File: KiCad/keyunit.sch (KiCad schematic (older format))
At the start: 22 parts, among them J1 Conn_01x03_Male, J2 Conn_01x02_Male, J3 Conn_01x05_Male, J4 Conn_01x04_Male, J5 Conn_01x05_Male, J6 Conn_01x04_Male, J8 Conn_01x02_Male, SW0 SW_Push, SW1 SW_Push, U1 test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

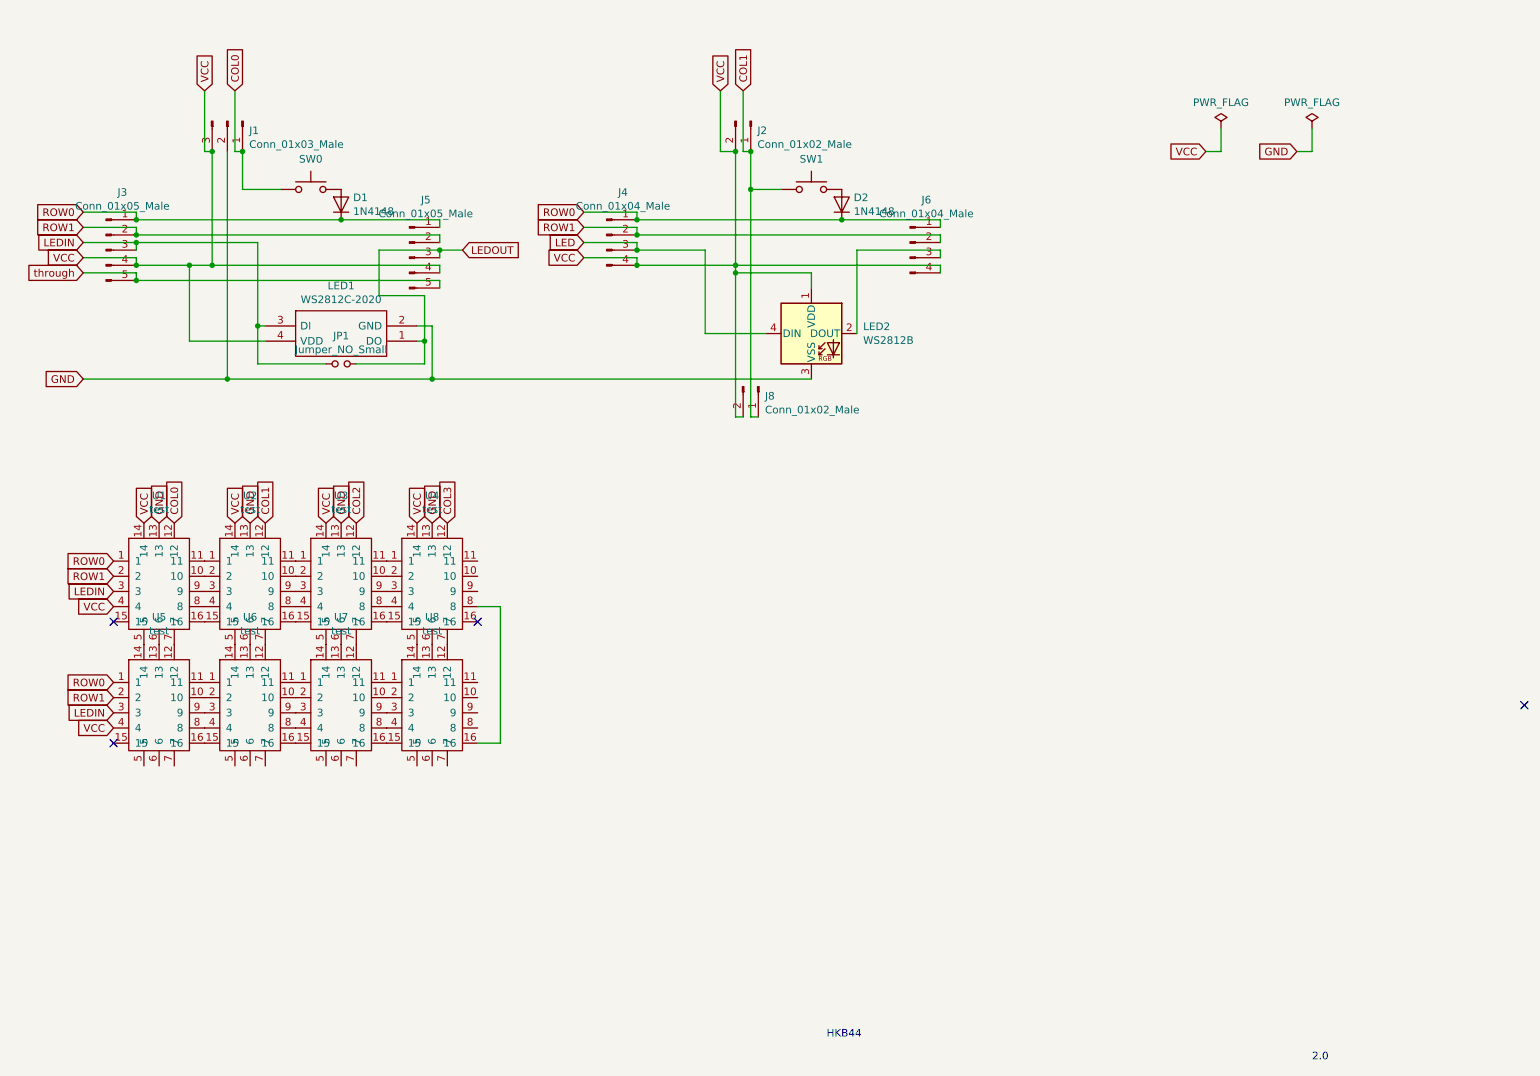
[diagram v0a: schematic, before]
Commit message: Add keyunit foot print and keyunit2 board
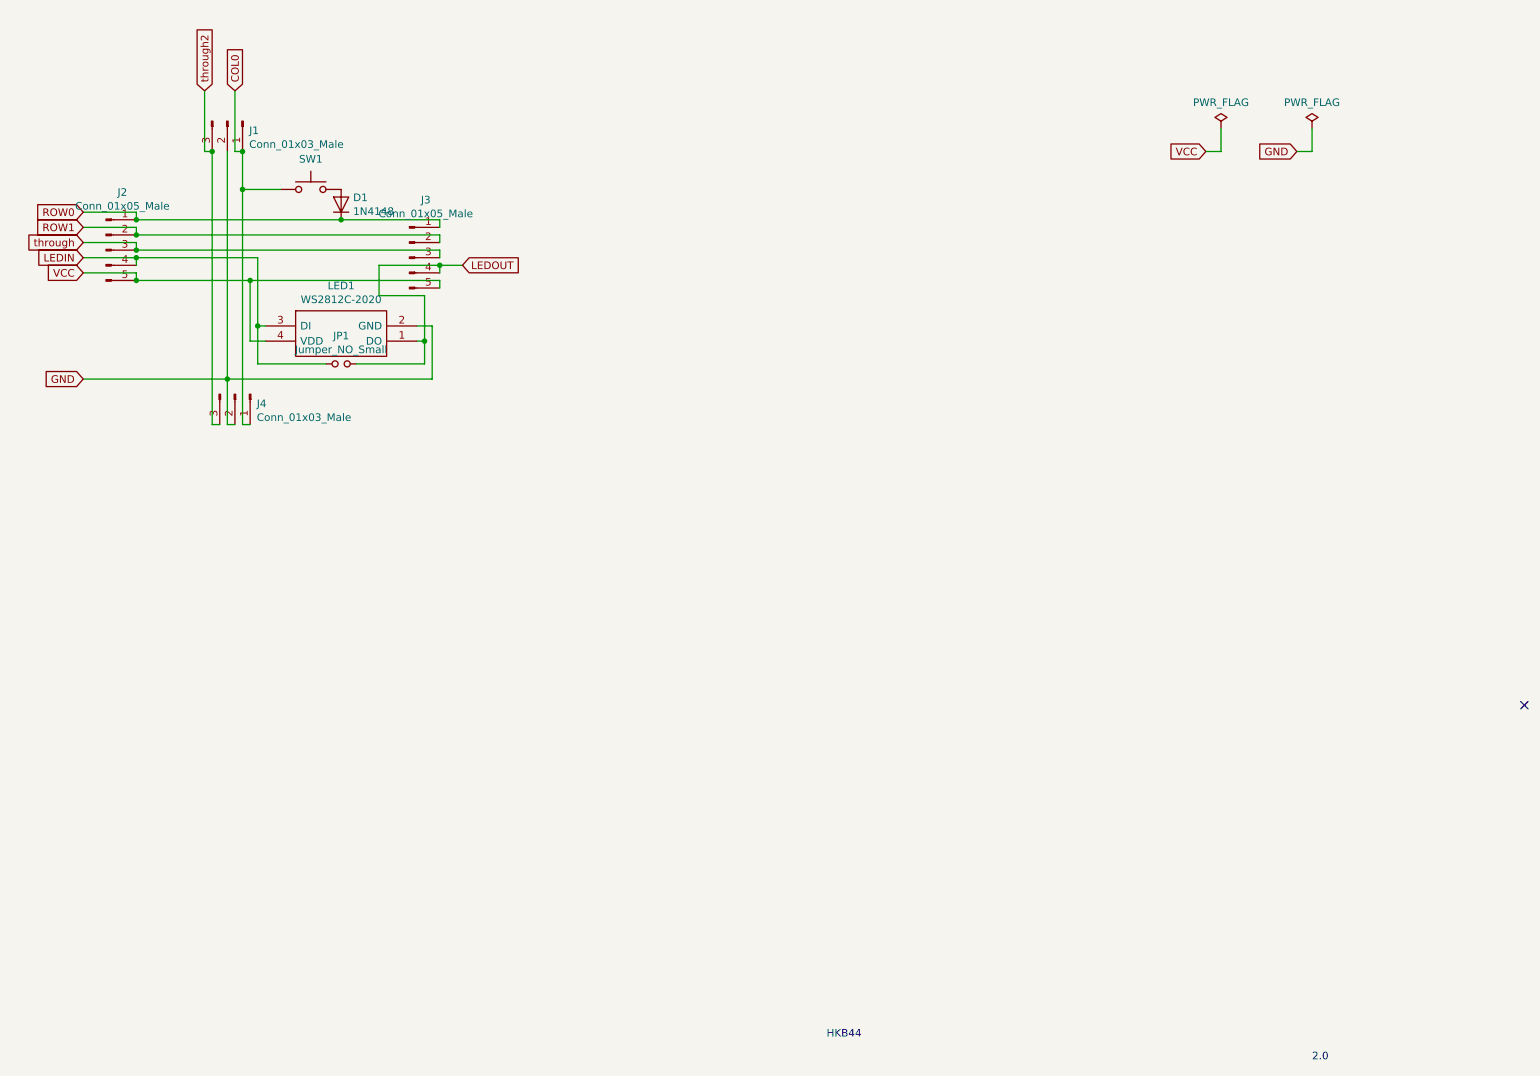
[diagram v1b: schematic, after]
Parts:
- removed D2: 1N4148, Diode_SMD:D_SOD-323_HandSoldering, symbol HKB44-rescue:1N4148-mod_1n148
- removed J2, J8: Conn_01x02_Male, Connector_PinHeader_2.54mm:PinHeader_1x02_P2.54mm_Vertical, symbol Connector:Conn_01x02_Male
- removed J4, J6: Conn_01x04_Male, Connector_PinHeader_2.54mm:PinHeader_1x04_P2.54mm_Vertical, symbol Connector:Conn_01x04_Male
- removed LED2: WS2812B, LED_SMD:LED_SK6812MINI_PLCC4_3.5x3.5mm_P1.75mm, symbol LED:WS2812B
- removed SW1: SW_Push, HKB44:MX_PCB_100H_socket, symbol Switch:SW_Push
- removed U1, U2, U3, U4, U5, U6, U7, U8: test, library:test, symbol mylib:test
- added J4: Conn_01x03_Male, Connector_PinHeader_2.54mm:PinHeader_1x03_P2.54mm_Vertical, symbol Connector:Conn_01x03_Male
- JP1: footprint Jumper:SolderJumper-2_P1.3mm_Open_TrianglePad1.0x1.5mm -> library:SolderJumper-2_small
- renumbered J3 to J2, J5 to J3, SW0 to SW1
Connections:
- net COL0: now also J4.1 (Pin_1)
- net GND: now also J4.2 (Pin_2)
- net LEDIN: now also J2.4 (Pin_4); no longer J2.3 (Pin_3)
- net LEDOUT: now also J3.4 (Pin_4); no longer J3.3 (Pin_3)
- net VCC: now also J2.5 (Pin_5), J3.5 (Pin_5); no longer J1.3 (Pin_3), J2.4 (Pin_4), J3.4 (Pin_4)
- net through: now also J2.3 (Pin_3), J3.3 (Pin_3); no longer J2.5 (Pin_5), J3.5 (Pin_5)
- new net through2: J1.3 (Pin_3), J4.3 (Pin_3)
- no-connect marks 4 -> 1
